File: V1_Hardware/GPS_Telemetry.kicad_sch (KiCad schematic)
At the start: 12 parts, among them J5 Conn_Coaxial, U10 NEO-M9N

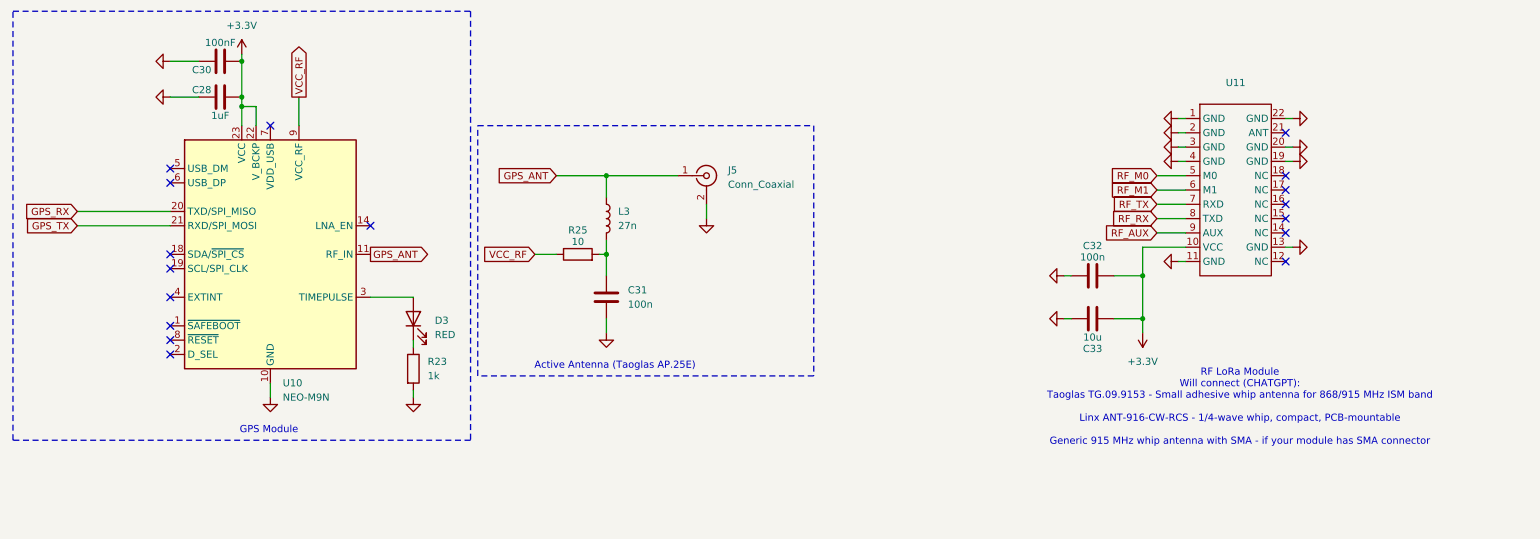
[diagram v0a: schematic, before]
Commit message: added the V1 to personal repo from org repo
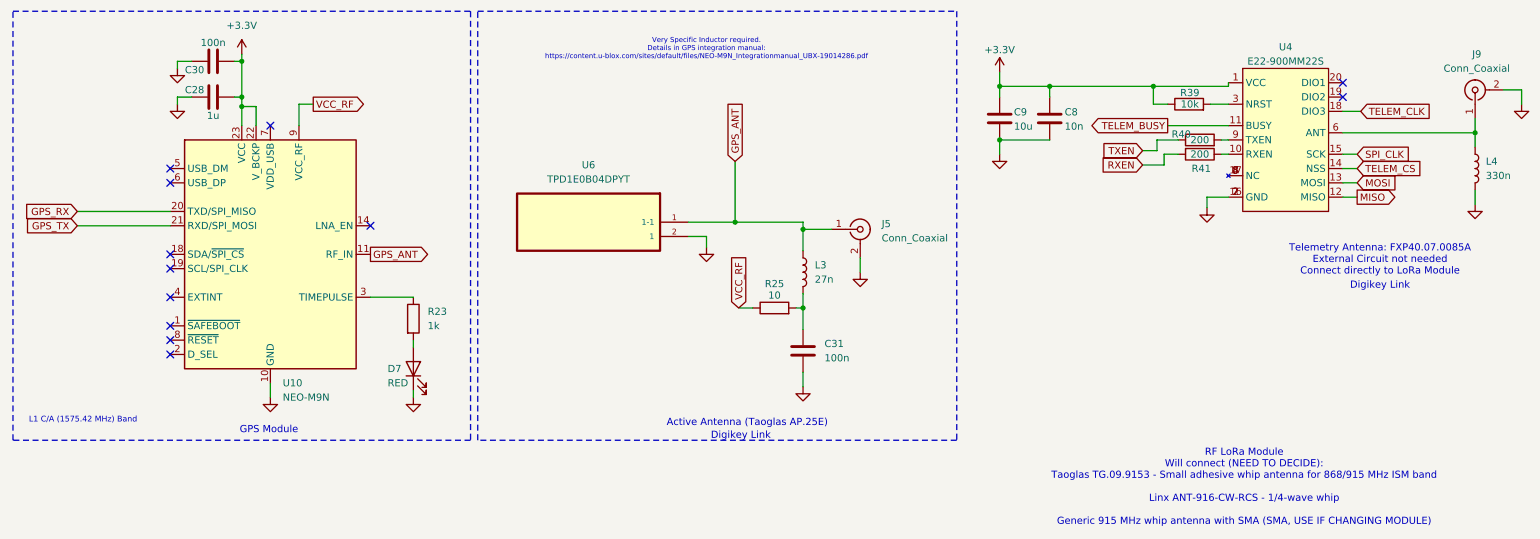
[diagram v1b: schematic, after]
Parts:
- removed C32: 100n, symbol Device:C
- removed C33: 10u, symbol Device:C
- removed D3: RED, symbol Device:LED
- removed U11: ~, ProLib_pcs_2025-08-31:WIRELM-SMD_E220-900T22S, symbol E220-900T22S:E220-900T22S
- added C8: 10n, Capacitor_SMD:C_0603_1608Metric_Pad1.08x0.95mm_HandSolder, symbol Device:C
- added C9: 10u, Capacitor_SMD:C_0603_1608Metric_Pad1.08x0.95mm_HandSolder, symbol Device:C
- added D7: RED, LED_SMD:LED_1206_3216Metric_Pad1.42x1.75mm_HandSolder, symbol Device:LED
- added J9: Conn_Coaxial, Connector_Coaxial:U.FL_Molex_MCRF_73412-0110_Vertical, symbol Connector:Conn_Coaxial
- added L4: 330n, Inductor_SMD:L_1008_2520Metric_Pad1.43x2.20mm_HandSolder, symbol Device:L
- added R39: 10k, Resistor_SMD:R_0603_1608Metric_Pad0.98x0.95mm_HandSolder, symbol Device:R
- added R40, R41: 200, Resistor_SMD:R_0603_1608Metric_Pad0.98x0.95mm_HandSolder, symbol Device:R
- added U4: E22-900MM22S, V1:E22-900MM22S, symbol E22-900MM22S:E22-900MM22S
- added U6: TPD1E0B04DPYT, V1:TPD1E0B04DPYT, symbol TPD1E0B04DPYT:TPD1E0B04DPYT
- C28: value 1uF -> 1u; footprint (none) -> Capacitor_SMD:C_0603_1608Metric_Pad1.08x0.95mm_HandSolder
- C30: value 100nF -> 100n; footprint (none) -> Capacitor_SMD:C_0603_1608Metric_Pad1.08x0.95mm_HandSolder
- C31: footprint (none) -> Capacitor_SMD:C_0603_1608Metric_Pad1.08x0.95mm_HandSolder
- J5: footprint (none) -> Connector_Coaxial:U.FL_Molex_MCRF_73412-0110_Vertical
- L3: footprint (none) -> Inductor_SMD:L_1008_2520Metric_Pad1.43x2.20mm_HandSolder
- R23, R25: footprint (none) -> Resistor_SMD:R_0603_1608Metric_Pad0.98x0.95mm_HandSolder
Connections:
- net +3.3V: now also C8.1, C9.1, R39.1, U4.1 (VCC)
- net GND: now also C8.2, C9.2, D7.1 (K), J9.2 (Ext), L4.2, U4.16 (GND), U4.2 (GND), U4.7 (GND), U6.2 (1); no longer R23.2
- net GPS_ANT: now also U6.1 (1-1)
- net at R23.1: now also U10.3 (TIMEPULSE)
- new net: J9.1 (In), L4.1, U4.6 (ANT)
- new net: D7.2 (A), R23.2
- new net: R40.2, U4.9 (TXEN)
- new net: R39.2, U4.3 (NRST)
- new net: R41.1, U4.10 (RXEN)
- new net: U4.17 (NC), U4.4 (NC), U4.5 (NC), U4.8 (NC)
- new net MISO: U4.12 (MISO)
- new net MOSI: U4.13 (MOSI)
- new net RXEN: R41.2
- new net SPI_CLK: U4.15 (SCK)
- new net TELEM_BUSY: U4.11 (BUSY)
- new net TELEM_CLK: U4.18 (DIO3)
- new net TELEM_CS: U4.14 (NSS)
- new net TXEN: R40.1
- no-connect marks 17 -> 12
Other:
- note added: "Digikey Link"
- note added: "L1 C/A (1575.42 MHz) Band"
- note added: "RF LoRa Module Will connect (NEED TO DECIDE): Taoglas TG.09.9153 - Small adhesive whip antenna for 868/915 MHz ISM band Linx ANT-916-CW-RCS - 1/4-wave whip Generic 915 MHz whip antenna with SMA (SMA, USE IF CHANGING MODULE)"
- note added: "Telemetry Antenna: FXP40.07.0085A External Circuit not needed Connect directly to LoRa Module"
- note added: "Very Specific Inductor required. Details in GPS integration manual: https://content.u-blox.com/sites/default/files/NEO-M9N_Integrationmanual_UBX-19014286.pdf"
- note removed: "RF LoRa Module Will connect (CHATGPT): Taoglas TG.09.9153 - Small adhesive whip antenna for 868/915 MHz ISM band Linx ANT-916-CW-RCS - 1/4-wave whip, compact, PCB-mountable Generic 915 MHz whip antenna with SMA - if your module has SMA connector"
- moved on the sheet: C28, C30, C31, J5, L3, R25
